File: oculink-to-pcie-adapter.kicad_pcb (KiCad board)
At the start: 2 copper layers, 0 parts

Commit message: [#79026] Add OCuLink and PCIex16 connectors, connect them together
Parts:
- added J1: OCuLink_x4_Amphenol_G14A421211112HR, antmicro-footprints:Amphenol_G14A421211112HR, F.Cu at (127.8, 112.1)
- added J2: PCIe_x16_10146070-113Y0LF-vertical, antmicro-footprints:AMPHENOL_10146070-113Y0LF, F.Cu at (137.5, 88.9)
- added MP1: MP_Pad6mm_Drill3.2mm, antmicro-footprints:MP_Pad6mm_Drill3.2mm, F.Cu at (70.0, 92.8)
- added MP2: MP_Pad6mm_Drill3.2mm, antmicro-footprints:MP_Pad6mm_Drill3.2mm, F.Cu at (70.0, 100.4)
- added MP3: MP_Pad6mm_Drill3.2mm, antmicro-footprints:MP_Pad6mm_Drill3.2mm, F.Cu at (70.0, 108.0)
- added MP4: MP_Pad6mm_Drill3.2mm, antmicro-footprints:MP_Pad6mm_Drill3.2mm, F.Cu at (70.0, 115.5)

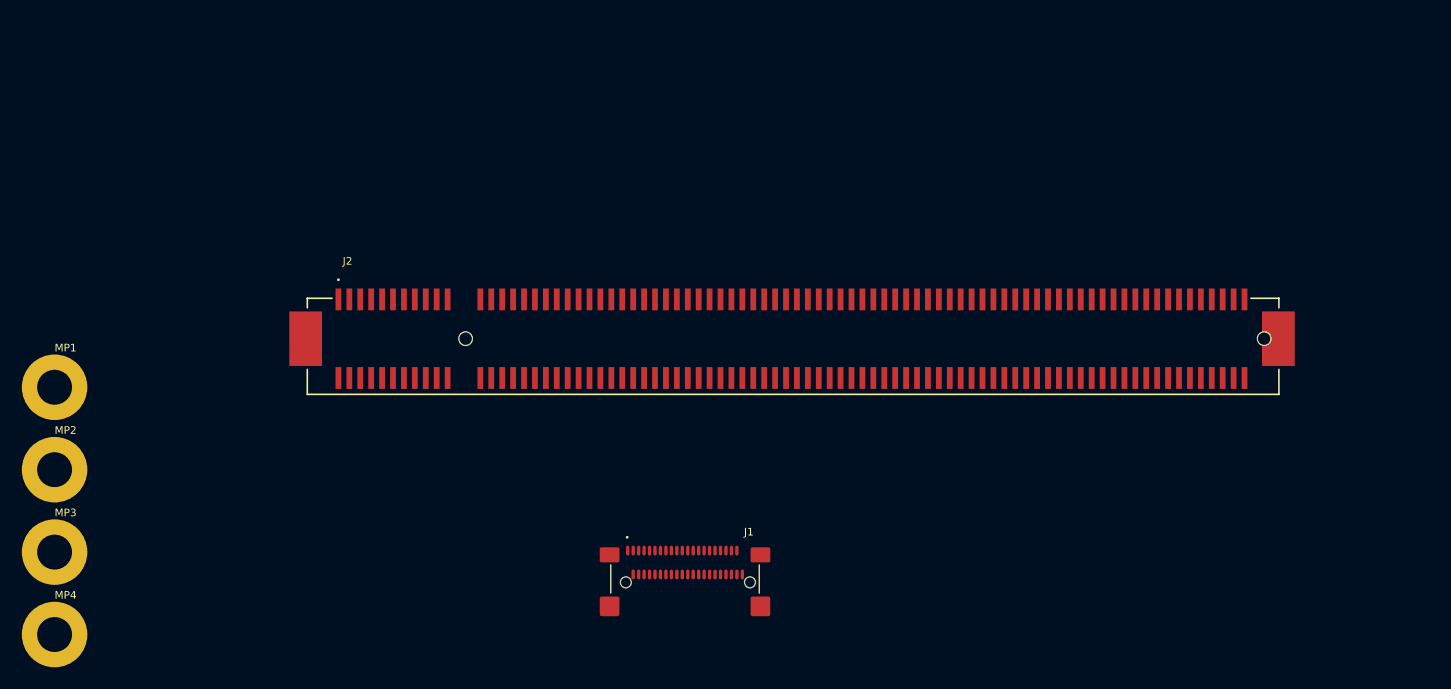
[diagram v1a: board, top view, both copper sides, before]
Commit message: [#79262] Begin component placement, add 12V PCIe decoupling capacitors, reduce inductor size
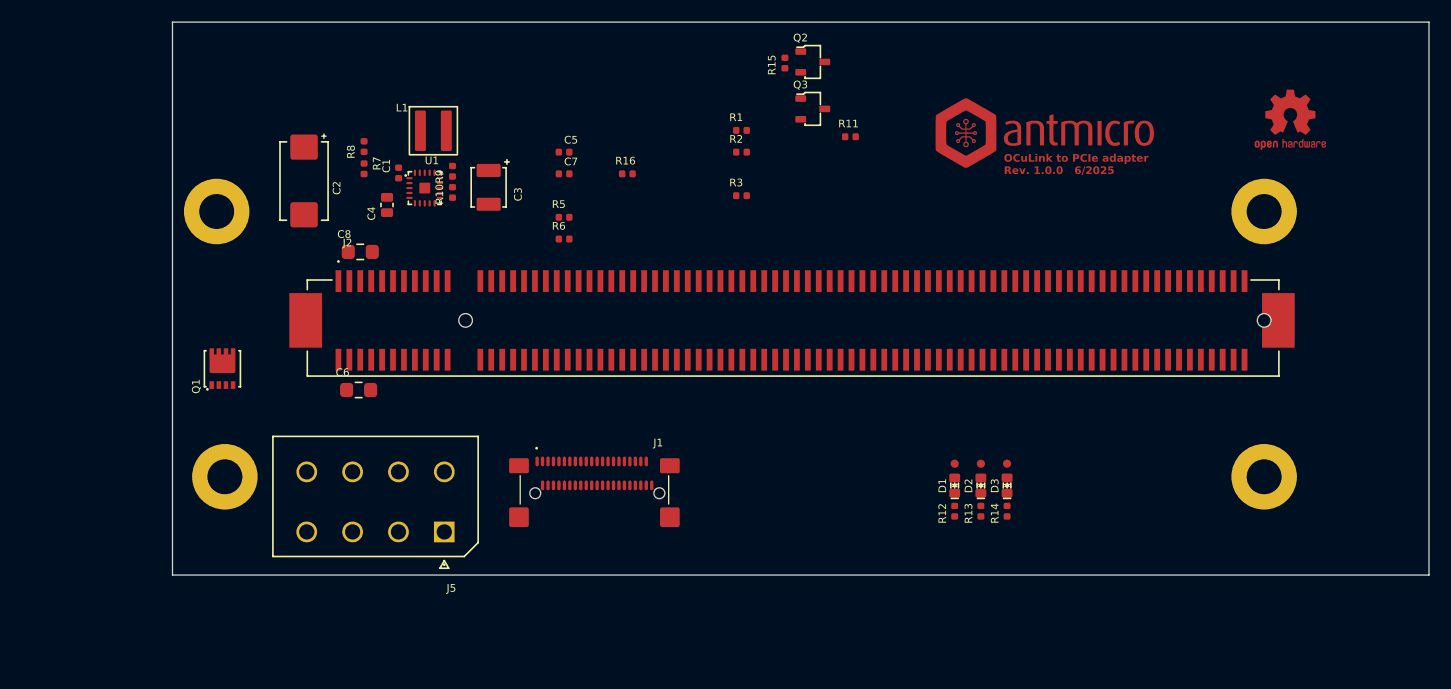
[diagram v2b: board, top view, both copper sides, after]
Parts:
- added C1: C_100n_0402, antmicro-footprints:C_0402_1005Metric, F.Cu at (101.5, 73.2)
- added C2: C_Pol_68u_16V_Panasonic-TQC-D, antmicro-footprints:C_Pol_EIA-D, F.Cu at (92.8, 74.0)
- added C3: C_Pol_100u_10V_KEMET-T520-B, antmicro-footprints:C_Pol_EIA-B, F.Cu at (109.8, 74.5)
- added C4: C_22u_16V_0603, antmicro-footprints:C_0603_1608Metric_EIA, F.Cu at (100.5, 76.2)
- added C5: C_1u_0402, antmicro-footprints:C_0402_1005Metric, F.Cu at (116.7, 71.3)
- added C6: C_10u_0805_35V, antmicro-footprints:C_0805_2012Metric, F.Cu at (97.8, 93.1)
- added C7: C_1u_0402, antmicro-footprints:C_0402_1005Metric, F.Cu at (116.7, 73.3)
- added C8: C_10u_0805_35V, antmicro-footprints:C_0805_2012Metric, F.Cu at (98.0, 80.5)
- added D1: LED_G_0603_LTST-C190GKT, antmicro-footprints:LED_0603_1608Metric_G, F.Cu at (152.4, 101.8)
- added D2: LED_G_0603_LTST-C190GKT, antmicro-footprints:LED_0603_1608Metric_G, F.Cu at (154.8, 101.8)
- added D3: LED_G_0603_LTST-C190GKT, antmicro-footprints:LED_0603_1608Metric_G, F.Cu at (157.2, 101.8)
- added J5: Molex_Mini-Fit-Jr_2x4_39-28-8080, antmicro-footprints:MOLEX_39288080, F.Cu at (105.7, 106.1)
- added L1: L_1u8_6.8A_WE-MAPI-4020, antmicro-footprints:L_WE-MAPI-4020, F.Cu at (104.7, 69.3)
- added Q1: DMPH4029LFGQ, antmicro-footprints:PowerDI3333-8, F.Cu at (85.4, 91.2)
- added Q2: BSS138-7-F, antmicro-footprints:SOT-23-3, F.Cu at (139.4, 63.1)
- added Q3: BSS138-7-F, antmicro-footprints:SOT-23-3, F.Cu at (139.4, 67.4)
- added R1: R_0R_0402, antmicro-footprints:R_0402_1005Metric, F.Cu at (132.9, 69.3)
- added R10: R_15k_0402, antmicro-footprints:R_0402_1005Metric, F.Cu at (106.5, 75.0)
- added R11: R_10k_0402, antmicro-footprints:R_0402_1005Metric, F.Cu at (142.9, 69.9)
- added R12: R_10k_0402, antmicro-footprints:R_0402_1005Metric, F.Cu at (152.4, 104.2)
- added R13: R_10k_0402, antmicro-footprints:R_0402_1005Metric, F.Cu at (154.8, 104.2)
- added R14: R_10k_0402, antmicro-footprints:R_0402_1005Metric, F.Cu at (157.2, 104.2)
- added R15: R_100k_0402, antmicro-footprints:R_0402_1005Metric, F.Cu at (136.9, 63.1)
- added R16: R_10k_0402, antmicro-footprints:R_0402_1005Metric, F.Cu at (122.5, 73.3)
- added R2: R_0R_0402, antmicro-footprints:R_0402_1005Metric, F.Cu at (132.9, 71.3)
- added R3: R_0R_0402, antmicro-footprints:R_0402_1005Metric, F.Cu at (132.9, 75.3)
- added R5: R_68k_0402, antmicro-footprints:R_0402_1005Metric, F.Cu at (116.7, 77.3)
- added R6: R_10k_0402, antmicro-footprints:R_0402_1005Metric, F.Cu at (116.7, 79.3)
- added R7: R_10k_0402, antmicro-footprints:R_0402_1005Metric, F.Cu at (98.3, 72.8)
- added R8: R_15k_0402, antmicro-footprints:R_0402_1005Metric, F.Cu at (98.3, 70.8)
- added R9: R_68k_0402, antmicro-footprints:R_0402_1005Metric, F.Cu at (106.5, 73.1)
- added REF**: antmicro-logo_scaled_20mm, antmicro-footprints:antmicro-logo_scaled_20mm, F.Cu at (160.7, 69.8)
- added REF**: OSHW-Logo2_7.3x6mm_Copper_Mask, antmicro-footprints:OSHW-Logo2_7.3x6mm_Copper_Mask, F.Cu at (183.2, 68.3)
- added TP1: TP_0.75mm_SMD, antmicro-footprints:TP_SMD_0.75mm, F.Cu at (152.4, 99.8)
- added TP2: TP_0.75mm_SMD, antmicro-footprints:TP_SMD_0.75mm, F.Cu at (154.8, 99.8)
- added TP3: TP_0.75mm_SMD, antmicro-footprints:TP_SMD_0.75mm, F.Cu at (157.2, 99.8)
- added U1: TPS56C230, antmicro-footprints:QFN-20-1EP_3x3mm_P0.45mm, F.Cu at (103.9, 74.6)
- moved MP1 112.0 mm to (180.8, 76.8)
- moved MP4 111.7 mm to (180.8, 101.0)
- moved MP2 27.9 mm to (84.8, 76.8)
- moved MP3 17.1 mm to (85.6, 101.0)
- moved J1 11.6 mm to (119.5, 104.0)
- moved J2 1.67 mm to (137.5, 87.2)
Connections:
- J1 pad A10: unconnected-(J1-~{CWAKE}-PadA10) -> Net-(J1-SDA)
- J1 pad A12: unconnected-(J1-VSP1-PadA12) -> /OCuLink/~{PERST}
- J1 pad A13: unconnected-(J1-VSP2-PadA13) -> /OCuLink/~{CPRSNT}
- J1 pad A15: /OCuLink/PCIe_{x4}.RX2+ -> /OCuLink/PCIe_{x4}.TX2+
- J1 pad A16: /OCuLink/PCIe_{x4}.RX2- -> /OCuLink/PCIe_{x4}.TX2-
- J1 pad A18: /OCuLink/PCIe_{x4}.RX3+ -> /OCuLink/PCIe_{x4}.TX3+
- J1 pad A19: /OCuLink/PCIe_{x4}.RX3- -> /OCuLink/PCIe_{x4}.TX3-
- J1 pad A21: Net-(J1-5V-PadA21) -> unconnected-(J1-V_{ACT}_TX_3V3-PadA21)
- J1 pad A3: /OCuLink/PCIe_{x4}.RX0+ -> /OCuLink/PCIe_{x4}.TX0+
- J1 pad A4: /OCuLink/PCIe_{x4}.RX0- -> /OCuLink/PCIe_{x4}.TX0-
- J1 pad A6: /OCuLink/PCIe_{x4}.RX1+ -> /OCuLink/PCIe_{x4}.TX1+
- J1 pad A7: /OCuLink/PCIe_{x4}.RX1- -> /OCuLink/PCIe_{x4}.TX1-
- J1 pad A9: unconnected-(J1-NC-PadA9) -> Net-(J1-SCL)
- J1 pad B1: Net-(J1-5V-PadA21) -> unconnected-(J1-V_{ACT}_RX_3V3-PadB1)
- J1 pad B10: unconnected-(J1-SDA-PadB10) -> /OCuLink/~{WAKE}
- J1 pad B12: unconnected-(J1-~{PERST}-PadB12) -> /OCuLink/PCIe_{REF0}.CK+
- J1 pad B13: unconnected-(J1-~{CPRSNT}-PadB13) -> /OCuLink/PCIe_{REF0}.CK-
- J1 pad B15: /OCuLink/PCIe_{x4}.TX2+ -> /OCuLink/PCIe_{x4}.RX2+
- J1 pad B16: /OCuLink/PCIe_{x4}.TX2- -> /OCuLink/PCIe_{x4}.RX2-
- J1 pad B18: /OCuLink/PCIe_{x4}.TX3+ -> /OCuLink/PCIe_{x4}.RX3+
- J1 pad B19: /OCuLink/PCIe_{x4}.TX3- -> /OCuLink/PCIe_{x4}.RX3-
- J1 pad B3: /OCuLink/PCIe_{x4}.TX0+ -> /OCuLink/PCIe_{x4}.RX0+
- J1 pad B4: /OCuLink/PCIe_{x4}.TX0- -> /OCuLink/PCIe_{x4}.RX0-
- J1 pad B6: /OCuLink/PCIe_{x4}.TX1+ -> /OCuLink/PCIe_{x4}.RX1+
- J1 pad B7: /OCuLink/PCIe_{x4}.TX1- -> /OCuLink/PCIe_{x4}.RX1-
- J2 pad A10: unconnected-(J2-PadA10) -> +3V3_PCIE
- J2 pad A11: unconnected-(J2-PadA11) -> /OCuLink/~{PERST}
- J2 pad A13: unconnected-(J2-PadA13) -> /OCuLink/PCIe_{REF0}.CK+
- J2 pad A14: unconnected-(J2-PadA14) -> /OCuLink/PCIe_{REF0}.CK-
- J2 pad A16: unconnected-(J2-PadA16) -> /OCuLink/PCIe_{x4}.RX0+
- J2 pad A17: unconnected-(J2-PadA17) -> /OCuLink/PCIe_{x4}.RX0-
- J2 pad A2: unconnected-(J2-PadA2) -> +12V_PCIE
- J2 pad A21: unconnected-(J2-PadA21) -> /OCuLink/PCIe_{x4}.RX1+
- J2 pad A22: unconnected-(J2-PadA22) -> /OCuLink/PCIe_{x4}.RX1-
- J2 pad A25: unconnected-(J2-PadA25) -> /OCuLink/PCIe_{x4}.RX2+
- J2 pad A26: unconnected-(J2-PadA26) -> /OCuLink/PCIe_{x4}.RX2-
- J2 pad A29: unconnected-(J2-PadA29) -> /OCuLink/PCIe_{x4}.RX3+
- J2 pad A3: unconnected-(J2-PadA3) -> +12V_PCIE
- J2 pad A30: unconnected-(J2-PadA30) -> /OCuLink/PCIe_{x4}.RX3-
- J2 pad A9: unconnected-(J2-PadA9) -> +3V3_PCIE
- J2 pad B1: unconnected-(J2-PadB1) -> +12V_PCIE
- J2 pad B10: unconnected-(J2-PadB10) -> /PCIe-connector/3V3_PCIe_AUX
- J2 pad B11: unconnected-(J2-PadB11) -> /OCuLink/~{WAKE}
- J2 pad B14: unconnected-(J2-PadB14) -> /OCuLink/PCIe_{x4}.TX0+
- J2 pad B15: unconnected-(J2-PadB15) -> /OCuLink/PCIe_{x4}.TX0-
- J2 pad B19: unconnected-(J2-PadB19) -> /OCuLink/PCIe_{x4}.TX1+
- J2 pad B2: unconnected-(J2-PadB2) -> +12V_PCIE
- J2 pad B20: unconnected-(J2-PadB20) -> /OCuLink/PCIe_{x4}.TX1-
- J2 pad B23: unconnected-(J2-PadB23) -> /OCuLink/PCIe_{x4}.TX2+
- J2 pad B24: unconnected-(J2-PadB24) -> /OCuLink/PCIe_{x4}.TX2-
- J2 pad B27: unconnected-(J2-PadB27) -> /OCuLink/PCIe_{x4}.TX3+
- J2 pad B28: unconnected-(J2-PadB28) -> /OCuLink/PCIe_{x4}.TX3-
- J2 pad B3: unconnected-(J2-PadB3) -> +12V_PCIE
- J2 pad B5: unconnected-(J2-PadB5) -> /OCuLink/I2C0.SCL
- J2 pad B6: unconnected-(J2-PadB6) -> /OCuLink/I2C0.SDA
- J2 pad B8: unconnected-(J2-PadB8) -> +3V3_PCIE
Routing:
- added copper zone on In1.Cu, net GND
- added copper zone on In2.Cu, net GND
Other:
- board outline added: 115.1 x 50.6 mm
- copper layers 2 -> 4
- board text added: "OCuLink to PCIe adapter Rev. ${REVISION} 6/2025"

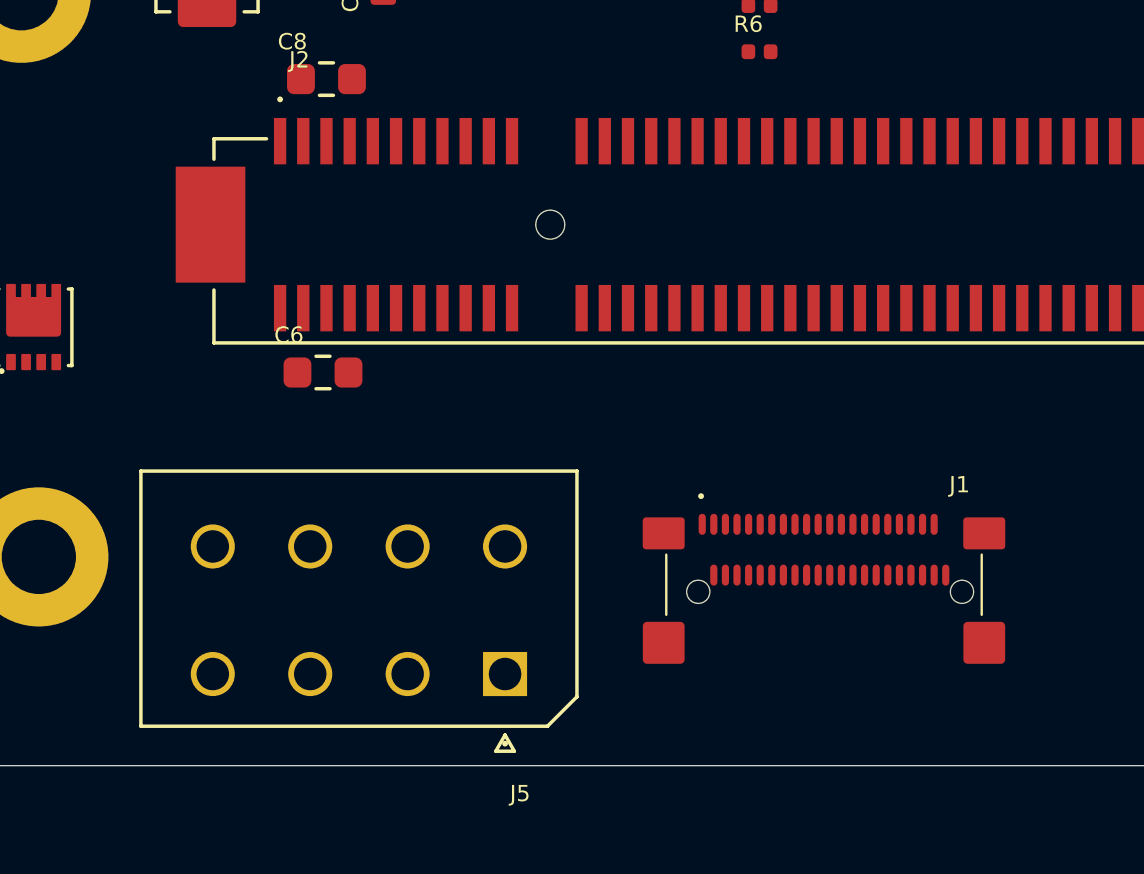
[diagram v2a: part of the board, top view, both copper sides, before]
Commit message: [#79262] Define stackup and PCIe differential pair parameters, start layout
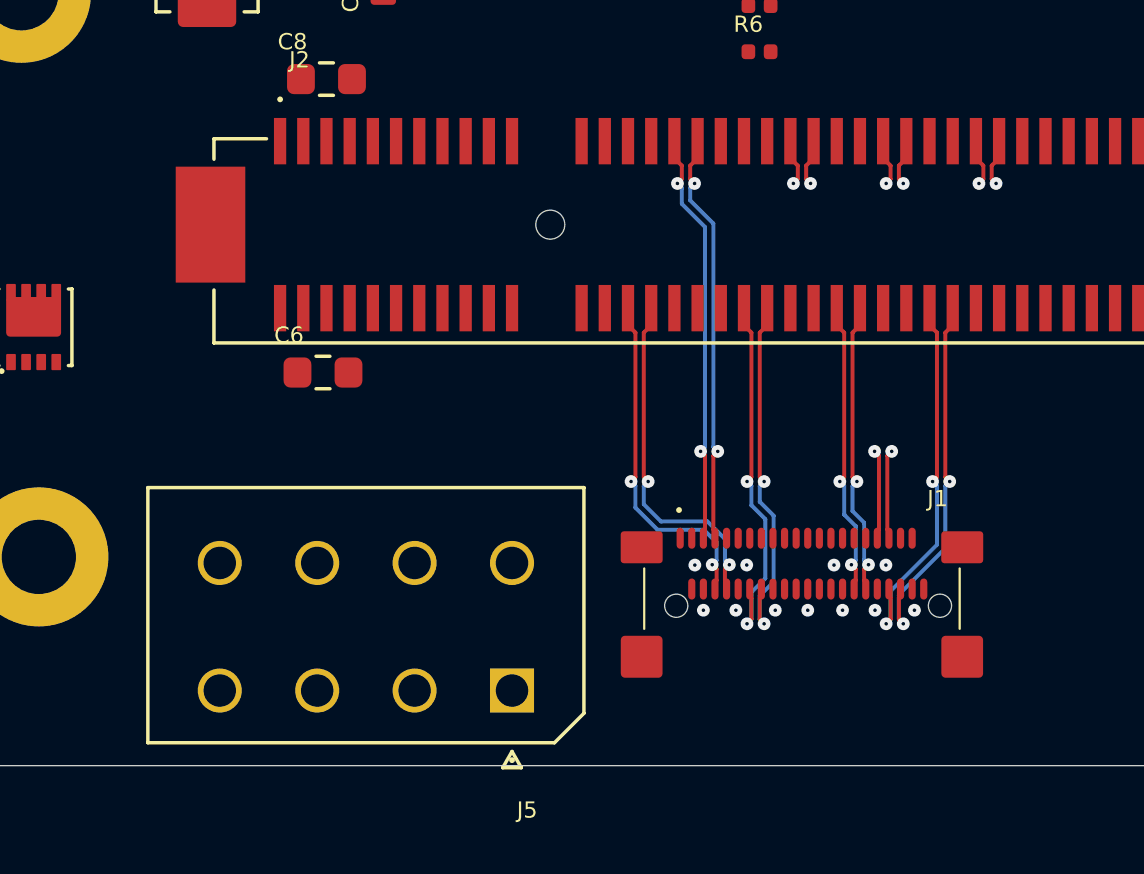
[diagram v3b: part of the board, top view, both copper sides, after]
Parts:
- moved J1 1.12 mm to (118.5, 104.5)
- moved J5 0.77 mm to (106.0, 106.8)
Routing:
- net /OCuLink/PCIe_{x4}.RX0-: track 0.00 -> 18.0 mm, vias 0 -> 2
- net /OCuLink/PCIe_{x4}.RX0+: track 0.00 -> 18.0 mm, vias 0 -> 2
- net /OCuLink/PCIe_{x4}.TX3+: track 0.00 -> 16.4 mm, vias 0 -> 2
- net /OCuLink/PCIe_{x4}.TX3-: track 0.00 -> 16.4 mm, vias 0 -> 2
- net /OCuLink/PCIe_{x4}.TX1-: track 0.00 -> 16.1 mm, vias 0 -> 2
- net /OCuLink/PCIe_{x4}.TX1+: track 0.00 -> 16.1 mm, vias 0 -> 2
- net /OCuLink/PCIe_{x4}.TX0-: track 0.00 -> 15.2 mm, vias 0 -> 2
- net /OCuLink/PCIe_{x4}.TX0+: track 0.00 -> 15.2 mm, vias 0 -> 2
- net /OCuLink/PCIe_{x4}.TX2-: track 0.00 -> 12.8 mm, vias 0 -> 2
- net /OCuLink/PCIe_{x4}.TX2+: track 0.00 -> 12.8 mm, vias 0 -> 2
- net /OCuLink/PCIe_{x4}.RX3-: track 0.00 -> 5.89 mm, vias 0 -> 2
- net /OCuLink/PCIe_{x4}.RX3+: track 0.00 -> 5.89 mm, vias 0 -> 2
- net /OCuLink/PCIe_{x4}.RX1-: track 0.00 -> 2.04 mm, vias 0 -> 1
- net /OCuLink/PCIe_{x4}.RX2-: track 0.00 -> 2.04 mm, vias 0 -> 1
- net /OCuLink/PCIe_{x4}.RX2+: track 0.00 -> 2.04 mm, vias 0 -> 1
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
